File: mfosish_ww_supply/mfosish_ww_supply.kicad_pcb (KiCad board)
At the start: 2 copper layers, 100 x 61 mm, 33 parts, among them J1 Conn_01x02, J2 Conn_01x03, J3 Conn_01x02, J4 Conn_01x03, U1 LM7812_TO220, U2 LM7912_TO220

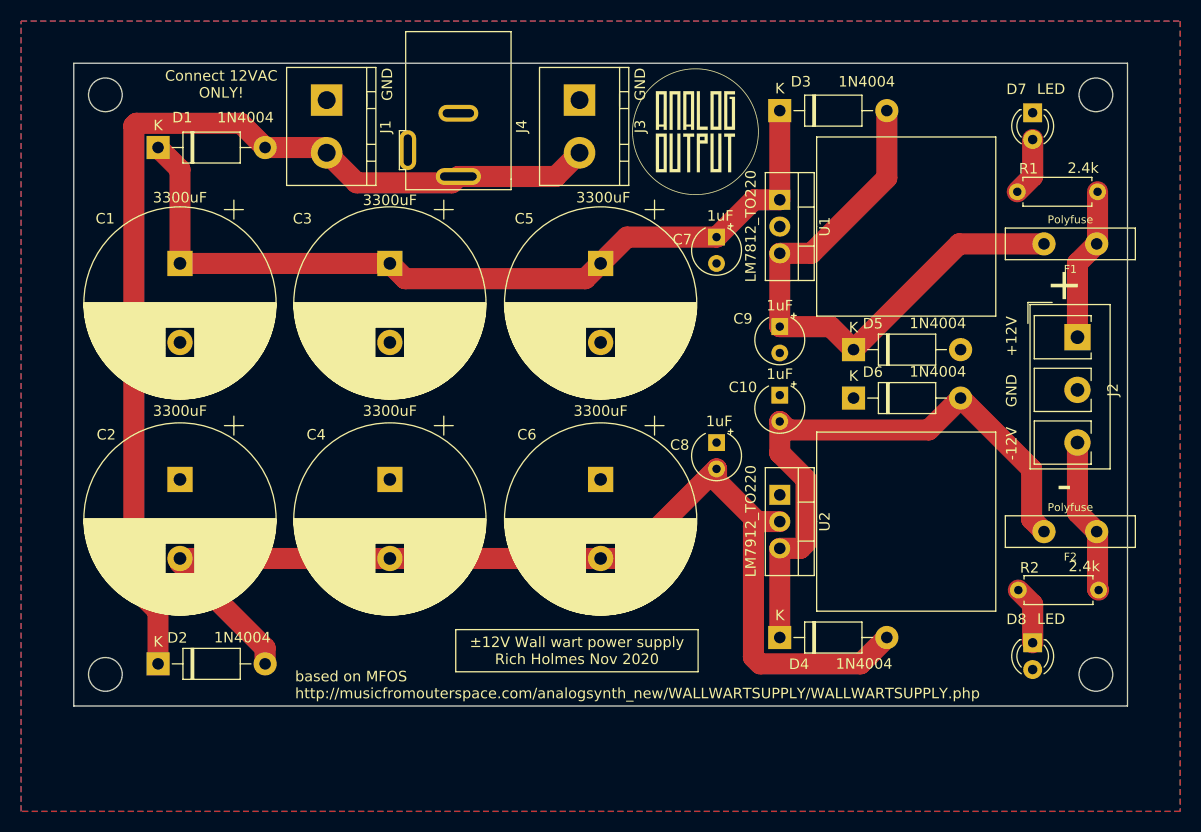
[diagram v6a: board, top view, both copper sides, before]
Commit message: Rotate pluggable blocks, some new footprints; holes, logo, heatsinks on schematic
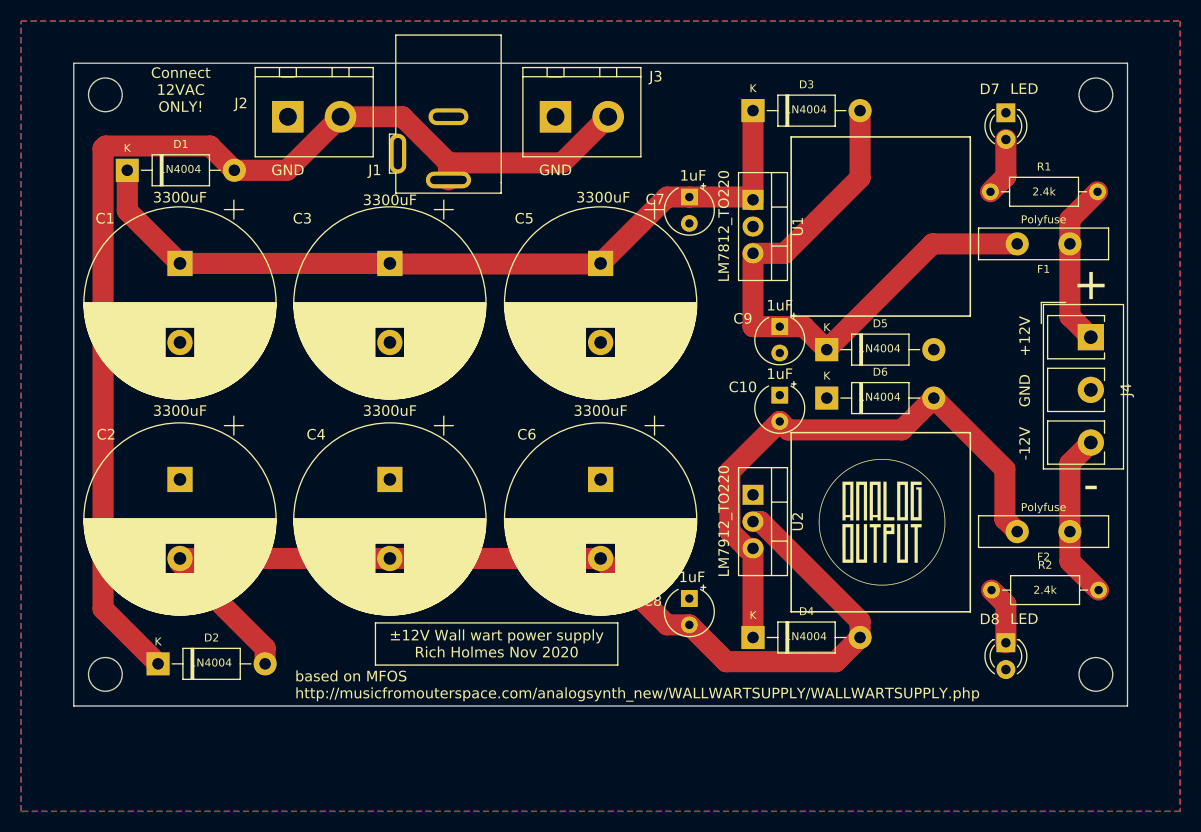
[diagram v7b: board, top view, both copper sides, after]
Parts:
- removed G***: LOGO, ao_tht:analogoutput_12mm
- removed REF** (x4): MountingHole_3.2mm_M3, ao_tht:MountingHole_3.2mm_M3
- added GRAF1: AO logo, ao_tht:analogoutput_12mm, F.Cu at (126.7, 107.6)
- added H1: MountingHole, ao_tht:MountingHole_3.2mm_M3, F.Cu at (53.0, 67.0)
- added H2: MountingHole, ao_tht:MountingHole_3.2mm_M3, F.Cu at (147.0, 67.0)
- added H3: MountingHole, ao_tht:MountingHole_3.2mm_M3, F.Cu at (53.0, 122.0)
- added H4: MountingHole, ao_tht:MountingHole_3.2mm_M3, F.Cu at (147.0, 122.0)
- added HS1: Heatsink, ao_tht:Heatsink_17x17mm_A-5093, F.Cu at (126.6, 79.5)
- added HS2: Heatsink, ao_tht:Heatsink_17x17mm_A-5093, F.Cu at (126.6, 107.6)
- D1, D2, D3, D4, D5, D6: footprint Diode_THT:D_DO-41_SOD81_P10.16mm_Horizontal -> ao_tht:D_DO-41_SOD81_P10.16mm_Horizontal
- R1, R2: footprint Resistor_THT:R_Axial_DIN0207_L6.3mm_D2.5mm_P7.62mm_Horizontal -> ao_tht:R_Axial_DIN0207_L6.3mm_D2.5mm_P10.16mm_Horizontal
- moved C8 15.0 mm to (108.4, 114.8)
- moved C7 4.59 mm to (108.4, 76.7)
- moved J2 4.00 mm to (70.3, 69.1), turned to 0 degrees
- moved D1 3.63 mm to (55.1, 74.2)
- moved J3 2.77 mm to (95.7, 69.1), turned to 0 degrees
- moved D3 2.54 mm to (114.5, 68.5)
- moved D4 2.54 mm to (114.5, 118.5)
- moved D5 2.54 mm to (121.5, 91.2)
- moved D6 2.54 mm to (121.5, 95.8)
- moved U1 2.54 mm to (114.5, 77.0)
- moved U2 2.54 mm to (114.5, 105.0)
- moved D7 2.54 mm to (138.5, 68.7)
- moved D8 2.54 mm to (138.5, 119.0)
- moved F1 2.54 mm to (142.0, 81.1)
- moved F2 2.54 mm to (142.0, 108.5)
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- renumbered J4 to J1, J1 to J2, J2 to J4
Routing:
- net Net-(D1-Pad2): track 97.9 -> 107.4 mm
- net Net-(C2-Pad2): track 103.5 -> 98.5 mm
- net Net-(C1-Pad1): track 81.0 -> 76.6 mm
- net Net-(C10-Pad2): track 58.4 -> 55.8 mm
- net -12V: track 14.8 -> 16.0 mm
- net +12V: track 14.6 -> 15.7 mm
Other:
- net class Default: trace_width 0.25 -> 2

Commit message: No, I liked the first orientation better
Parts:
- moved J3 5.24 mm to (100.8, 67.8), turned to 270 degrees
- moved J2 2.84 mm to (72.9, 67.8), turned to 270 degrees
- moved J1 2.65 mm to (88.1, 69.1)
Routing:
- net Net-(D1-Pad2): track 107.4 -> 103.7 mm
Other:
- board text added: "K"
